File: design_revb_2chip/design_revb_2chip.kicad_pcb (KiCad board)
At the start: 4 copper layers, 101.5 x 50.5 mm, 108 parts, among them J1 USB_C_Receptacle, J2 Conn_01x08, J3 09452812810, U1 LAN7801-I/9JX, U2 TPS62162QDSGRQ1, U3 93C56A-I/P, U4 DP83TG720SWRHARQ1, U5 TPS784105QWDRBRQ1, U6 219-5MST

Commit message: Semi-Final Fixes
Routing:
- net GPIO5: track 64.8 -> 64.0 mm
- net GND: vias 31 -> 34
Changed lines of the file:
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@@
 			)
 		)
-		(property "Footprint" "SW5_219SMT"
+		(property "Footprint" "Capstone_Footprints:SW5_219SMT"
 			(at 0 0 0)
 			(layer "F.Fab")
@@
 		(tags "resistor")
 		(property "Reference" "R23"
-			(at 0.5 2 360)
+			(at 0.5 2 0)
 			(layer "F.SilkS")
 			(effects
@@
 		)
 		(property "Value" "470"
-			(at 0 1.65 360)
+			(at 0 1.65 0)
 			(layer "F.Fab")
 			(effects
@@
 		)
 		(fp_text user "${REFERENCE}"
-			(at 0 0 360)
+			(at 0 0 0)
 			(layer "F.Fab")
 			(effects
@@
 		)
 		(property "Value" "470"
-			(at 0 1.65 360)
+			(at 0 1.65 0)
 			(layer "F.Fab")
 			(effects
@@
 		)
 		(fp_text user "${REFERENCE}"
-			(at 0 0 360)
+			(at 0 0 0)
 			(layer "F.Fab")
 			(effects
@@
 		(tags "resistor")
 		(property "Reference" "R22"
-			(at 0 1.5 360)
+			(at 0 1.5 0)
 			(layer "B.SilkS")
 			(effects
@@
 		)
 		(property "Value" "470"
-			(at 0 -1.65 360)
+			(at 0 -1.65 0)
 			(layer "B.Fab")
 			(effects
@@
 		)
 		(fp_text user "${REFERENCE}"
-			(at 0 0 360)
+			(at 0 0 0)
 			(layer "B.Fab")
 			(effects
@@
 		(tags "resistor")
 		(property "Reference" "R20"
-			(at 0 -2 360)
+			(at 0 -2 0)
 			(layer "B.SilkS")
 			(effects
@@
 		)
 		(property "Value" "2.2k"
-			(at 0 -1.65 360)
+			(at 0 -1.65 0)
 			(layer "B.Fab")
 			(effects
@@
 		)
 		(fp_text user "${REFERENCE}"
-			(at 0 0 360)
+			(at 0 0 0)
 			(layer "B.Fab")
 			(effects
@@
 	)
 	(via
+		(at 192 76)
+		(size 0.6)
+		(drill 0.3)
+		(layers "F.Cu" "B.Cu")
+		(net 1)
+	)
+	(via
+		(at 190.5 76)
+		(size 0.6)
+		(drill 0.3)
+		(layers "F.Cu" "B.Cu")
+		(net 1)
+	)
+	(via
 		(at 163.0875 86.5)
 		(size 0.6)
@@
 	)
 	(via
+		(at 189 76)
+		(size 0.6)
+		(drill 0.3)
+		(layers "F.Cu" "B.Cu")
+		(net 1)
+	)
+	(via
 		(at 176.5 79.5)
 		(size 0.6)
@@
 	)
 	(segment
-		(start 178 83)
+		(start 178 84.434315)
 		(end 178 90.5)
 		(width 0.2)
@@
 	)
 	(segment
-		(start 204.5 95.5)
-		(end 205 96)
-		(width 0.2)
-		(layer "B.Cu")
-		(net 36)
-	)
-	(segment
-		(start 175 81.5)
-		(end 176.5 81.5)
+		(start 178 90.5)
+		(end 183 95.5)
 		(width 0.2)
 		(layer "B.Cu")
@@
 	)
 	(segment
-		(start 178 90.5)
-		(end 183 95.5)
+		(start 204.5 95.5)
+		(end 205 96)
 		(width 0.2)
 		(layer "B.Cu")
@@
 	)
 	(segment
-		(start 190 95.5)
-		(end 204.5 95.5)
+		(start 175.065685 81.5)
+		(end 178 84.434315)
 		(width 0.2)
 		(layer "B.Cu")
@@
 	)
 	(segment
-		(start 176.5 81.5)
-		(end 178 83)
+		(start 183 95.5)
+		(end 204.5 95.5)
 		(width 0.2)
 		(layer "B.Cu")
@@
 	)
 	(segment
-		(start 183 95.5)
-		(end 190 95.5)
+		(start 175 81.5)
+		(end 175.065685 81.5)
 		(width 0.2)
 		(layer "B.Cu")

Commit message: PCB fixes
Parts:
- removed C11, C15, C9: 0.1uF, Capacitor_SMD:C_0201_0603Metric
- removed JP1, JP5: Jumper_2_Bridged, Jumper:SolderJumper-2_P1.3mm_Bridged_Pad1.0x1.5mm
- removed JP2, JP3, JP4: Jumper_2_Open, Jumper:SolderJumper-3_P1.3mm_Open_Pad1.0x1.5mm
- removed R1: 1k, Resistor_SMD:R_0805_2012Metric
- removed R5: 10k, Resistor_SMD:R_0805_2012Metric
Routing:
- net GND: track 337.1 -> 395.3 mm, vias 34 -> 74
- net TXD3: track 46.7 -> 27.7 mm
- net Net-(U2-EN): track 1.92 -> 11.6 mm
- net TXD2: track 33.7 -> 26.2 mm
- net /USB_SIDE/USB3_RXP: track 26.2 -> 30.1 mm
- net VBUS: track 17.1 -> 19.9 mm
- net /ETH_SIDE/Vdd1p0A: track 61.3 -> 62.1 mm
- net /ETH_SIDE/TRD_N: track 5.90 -> 6.49 mm
- net /ETH_SIDE/BI_DA-: track 20.9 -> 20.4 mm
- net /USB_SIDE/USB3_RXN: track 26.8 -> 26.7 mm, vias 2 -> 4

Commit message: Final PCB Fixes
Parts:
- removed J1: USB_C_Receptacle, Connector_USB:USB_C_Receptacle_Molex_105450-0101
- added C11: 0.1uF, Capacitor_SMD:C_0201_0603Metric, B.Cu at (181.3, 75.5)
- added C15: 0.1uF, Capacitor_SMD:C_0201_0603Metric, F.Cu at (194.0, 69.7)
- added C9: 0.1uF, Capacitor_SMD:C_0201_0603Metric, B.Cu at (181.7, 74.5)
- added J4: UJ31-CH-3-SMT-TR, Capstone_Footprints:CUI_UJ31-CH-3-SMT-TR, F.Cu at (157.1, 73.9)
- added R1: 1k, Resistor_SMD:R_0805_2012Metric, B.Cu at (198.9, 89.0)
- added R5: 10k, Resistor_SMD:R_0805_2012Metric, F.Cu at (183.6, 63.0)
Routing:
- net /USB_SIDE/USB3_TXN: track 27.6 -> 49.7 mm, vias 0 -> 1
- net /USB_SIDE/USB3_TXP: track 27.5 -> 47.8 mm, vias 0 -> 2
- net VDD33A: track 321.9 -> 341.2 mm, vias 19 -> 21
- net USB_SHIELD: track 36.9 -> 19.7 mm, vias 2 -> 0
- net GND: track 395.3 -> 405.5 mm, vias 74 -> 76
- net /USB_SIDE/USB3_RXP: track 30.1 -> 36.7 mm, vias 0 -> 1
- net /USB_SIDE/USB3_RXN: track 26.7 -> 31.9 mm, vias 4 -> 3
- net Net-(U1-EECS/GPIO0): track 22.9 -> 26.1 mm
- net MDIO: track 47.3 -> 49.9 mm
- net VBUS: track 19.9 -> 21.6 mm
- net VDD12A: track 48.9 -> 50.2 mm
- net /USB_SIDE/USB2_P: track 27.0 -> 27.6 mm, vias 2 -> 3

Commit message: PCB Fixes/Completion
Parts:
- J3: footprint Capstone_Footprints:09452812810 -> Capstone_Footprints:hartingt1; moved to F.Cu
- moved J3 2.80 mm to (244.3, 72.0), turned to 90 degrees
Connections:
- U2 pad V: (no net) -> GND
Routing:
- net GND: track 405.5 -> 409.3 mm, vias 76 -> 77

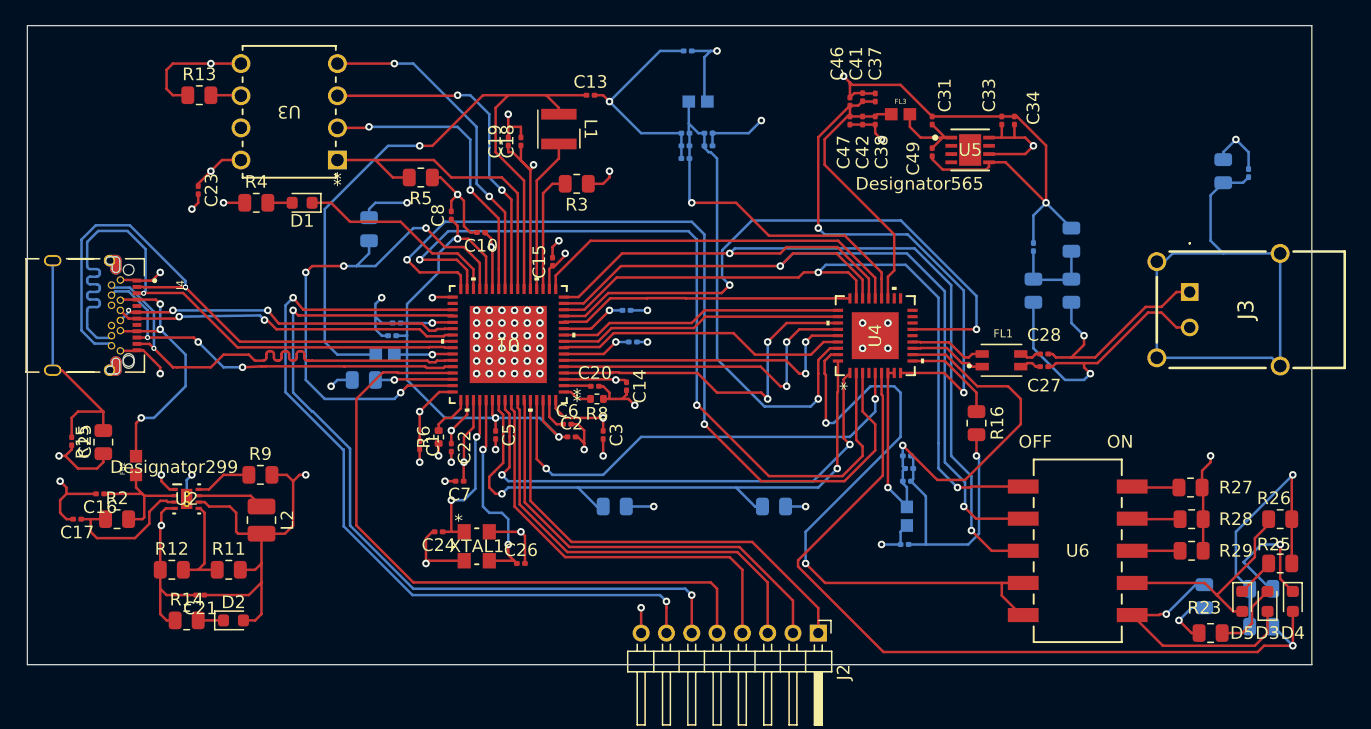
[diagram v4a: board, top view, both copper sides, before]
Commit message: Minor routing fixes + component resizing
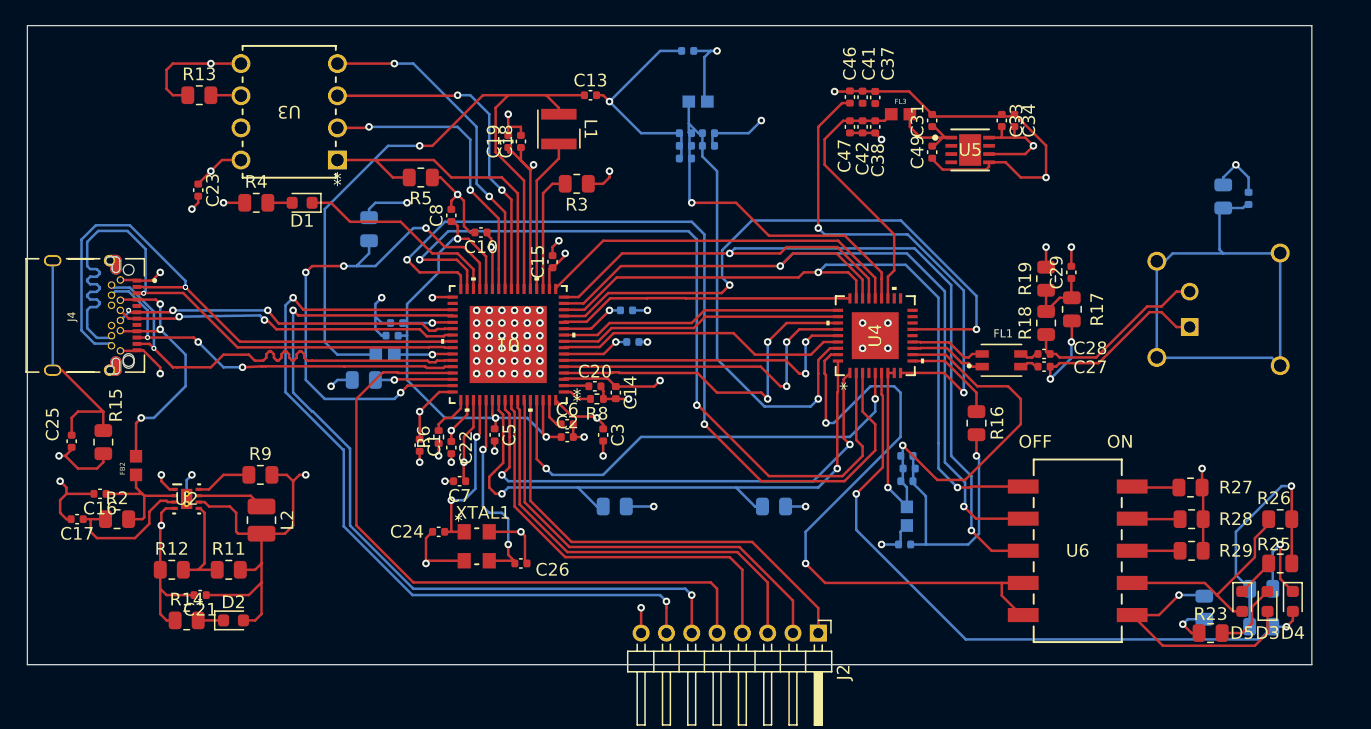
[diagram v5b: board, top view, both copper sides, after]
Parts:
- C1, C10, C11, C12, C13, C14, C15, C16, C17, C18, C19, C2, C20, C21, C22, C23, C24, C25, C26, C27, C28, C3, C30, C31, C32, C33, C34, C35, C36, C37, C38, C39, C4, C40, C41, C42, C43, C44, C45, C46, C47, C48, C49, C5, C50, C6, C7, C8, C9: footprint Capacitor_SMD:C_0201_0603Metric -> Capacitor_SMD:C_0402_1005Metric
- C29: footprint Capacitor_SMD:C_0201_0603Metric -> Capacitor_SMD:C_0402_1005Metric; moved to F.Cu
- J3: moved to B.Cu
- R17, R18, R19: moved to F.Cu
- moved R19 3.68 mm to (233.0, 71.0)
- moved C29 3.60 mm to (235.0, 70.5)
- moved R17 3.38 mm to (235.0, 73.4)
- moved R18 3.24 mm to (233.0, 74.5)
- moved J3 2.77 mm to (244.4, 74.8), turned to -90 degrees
- moved C50 2.00 mm to (249.0, 64.7)
- moved R30 2.00 mm to (247.0, 64.5)
- moved C14 0.98 mm to (199.0, 80.0)
- moved R21 0.91 mm to (245.5, 97.0)
- moved C38 0.50 mm to (219.5, 59.0)
- moved C42 0.50 mm to (218.5, 59.0)
- moved C47 0.50 mm to (217.5, 59.0)
- moved C46 0.36 mm to (217.5, 56.6)
- moved C2 0.34 mm to (195.2, 83.5)
- moved C5 0.08 mm to (189.4, 83.3)
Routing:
- net VDD33A: track 341.2 -> 137.4 mm
- net GND: track 409.3 -> 206.2 mm, vias 77 -> 79
- net /ETH_SIDE/LED_1: track 65.1 -> 53.0 mm, vias 1 -> 2
- net /ETH_SIDE/BI_DA+: track 25.6 -> 21.7 mm, vias 1 -> 2
- net /ETH_SIDE/BI_DA-: track 20.4 -> 17.0 mm, vias 1 -> 0
- net Net-(D4-K): track 10.8 -> 7.87 mm
- net Net-(J3-GND_1): track 45.1 -> 42.6 mm
- net /ETH_SIDE/Vdd1p0A: track 62.1 -> 59.7 mm
- net Net-(C29-Pad1): track 7.53 -> 5.70 mm
- net VDD12A: track 50.2 -> 49.2 mm
- net RXD3: track 30.3 -> 29.7 mm

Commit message: footprint resizing
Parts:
- added C45: 10nF, Capacitor_SMD:C_0603_1608Metric, F.Cu at (0.94, 0.48)
- C13, C16, C18, C21, C29, C3, C30, C32, C33, C34: footprint Capacitor_SMD:C_0402_1005Metric -> Capacitor_SMD:C_0603_1608Metric
- moved C34 2.29 mm to (232.0, 56.8)
- moved C33 1.96 mm to (230.4, 56.8)
- moved C3 1.54 mm to (199.5, 83.0)
- moved C29 0.73 mm to (235.0, 69.8)
- moved C18 0.72 mm to (191.8, 59.5)
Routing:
- net VDD33A: track 137.4 -> 142.1 mm
- net GND: track 206.2 -> 210.4 mm
- net /ETH_SIDE/Vdd1p0A: track 59.7 -> 63.4 mm

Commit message: Final Push for Rev A 1.0
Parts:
- removed the C45 at (0.94, 0.48)
- removed the C45 at (204.5, 61.5)
- added C45: 10nF, Capacitor_SMD:C_0402_1005Metric, B.Cu at (204.5, 61.5)
- C13, C16, C21, C33: footprint Capacitor_SMD:C_0603_1608Metric -> Capacitor_SMD:C_0805_2012Metric
- C3, C30, C32, C34: footprint Capacitor_SMD:C_0603_1608Metric -> Capacitor_SMD:C_0402_1005Metric
- C49: footprint Capacitor_SMD:C_0402_1005Metric -> Capacitor_SMD:C_0805_2012Metric
- L1: footprint Inductor_SMD_Wurth:L_Wurth_WE-LQSH-3012 -> Inductor_SMD:L_0603_1608Metric
- moved C32 2.15 mm to (223.7, 93.0)
- moved C49 1.84 mm to (223.0, 62.5)
- moved C13 1.38 mm to (196.1, 55.5)
- moved C33 0.92 mm to (229.5, 56.5)
- moved C21 0.65 mm to (166.8, 96.2)
- moved C3 0.50 mm to (199.0, 83.0)
- moved D2 0.50 mm to (168.8, 98.5)
- moved R14 0.50 mm to (165.1, 98.5)
- moved R5 0.50 mm to (183.1, 63.0)
- moved C34 0.30 mm to (232.0, 56.5)
- moved C9 0.20 mm to (181.5, 74.5)
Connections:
- U2 pad V: GND -> (no net)
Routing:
- net VDD33A: track 142.1 -> 143.4 mm
- net GND: track 210.4 -> 209.2 mm, vias 79 -> 80
- net VDD12: track 57.9 -> 56.8 mm
- net /ETH_SIDE/Vdd1.0: track 8.42 -> 9.20 mm
- net 5V: track 10.6 -> 9.93 mm
- net /ETH_SIDE/VddioA: track 62.0 -> 62.5 mm
- net Net-(U1-EECS/GPIO0): track 26.1 -> 25.6 mm
